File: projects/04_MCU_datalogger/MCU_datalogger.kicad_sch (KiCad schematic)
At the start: 25 parts, among them U1 24LC1025, U2 DS1337S_, U3 24LC1025, U4 ATMEGA328P-AU, Y1 32.768KHz, Y2 16MHz

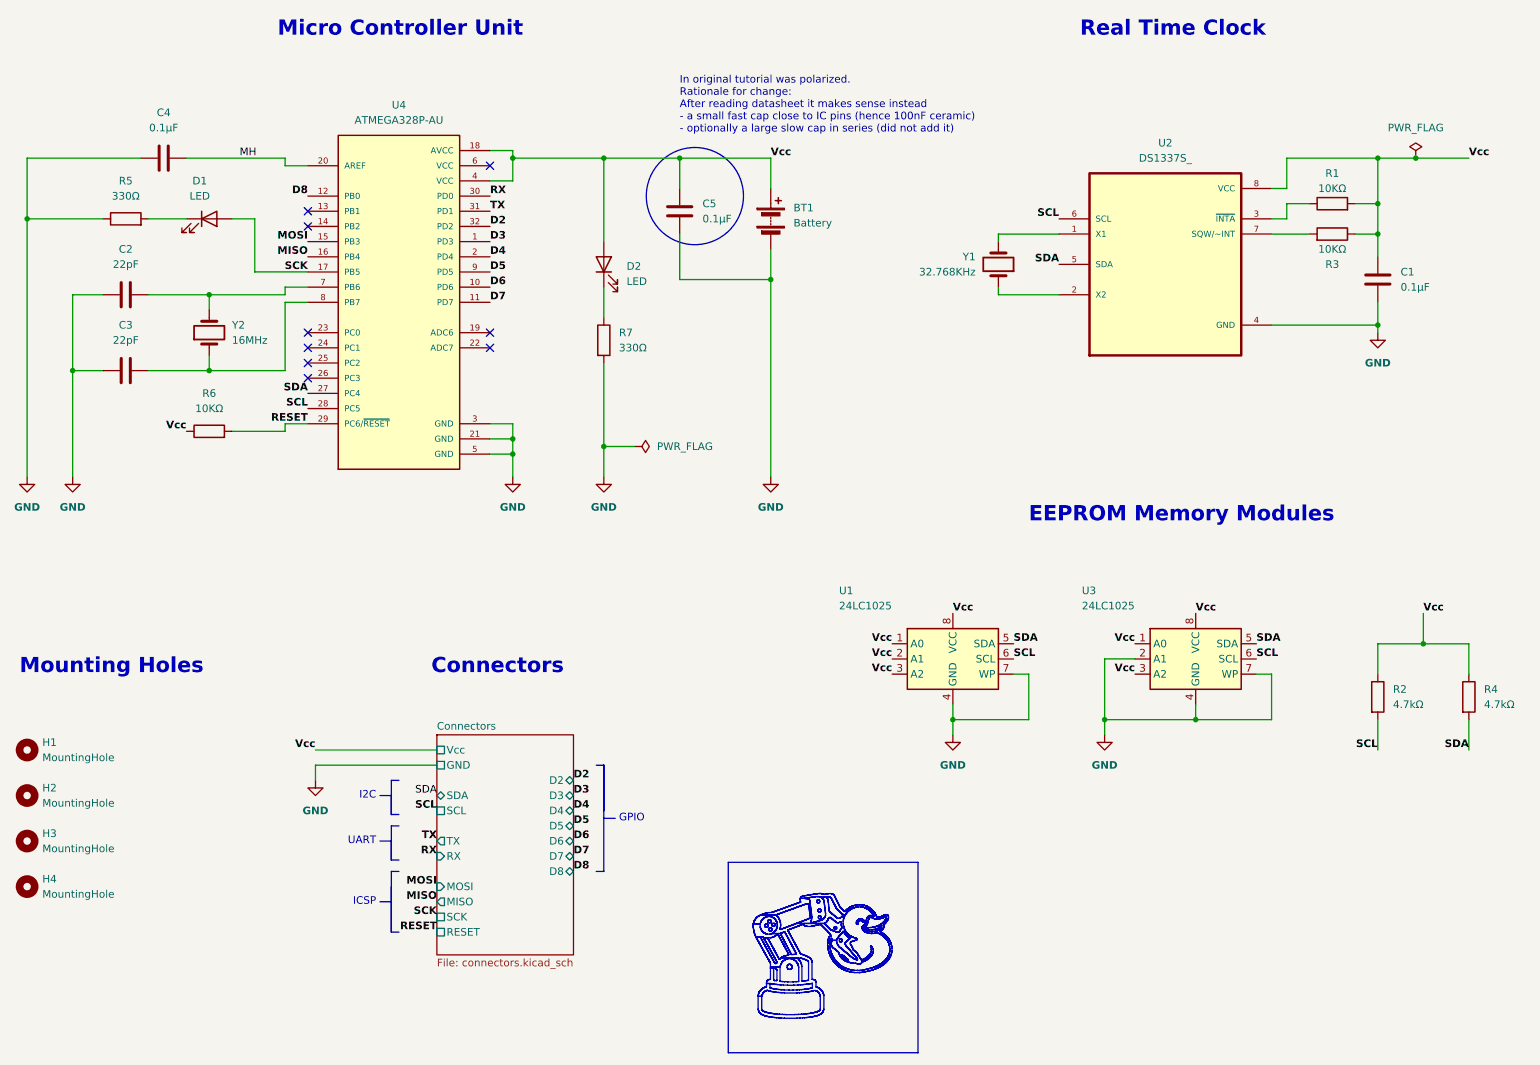
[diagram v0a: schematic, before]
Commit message: MCU datalogger - clean up schematic
In `MCU_datalogger.kicad_sch` and `connectors.kicad_sch`:
- update RTC, EEPROM, Crystal symbols to arrange pins properly
  and align to 100 mil grid
- clean up schematic
- rename nets to start with ICSP_* I2C_* UART_*
- replace Vcc label with VCC power symbol
- add net colors

In `MCU_datalogger.kicad_pcb`:
- replace layout in main branch with empty placeholder referring to 2layer and 4layer branches

Notes:
- ensure modified symbols are saved in custom library (e.g. MH_library)
- before deleting the layout DRC threw hundreds of errors: unconnected pins, solder mask bridges, etc. (WHY?)
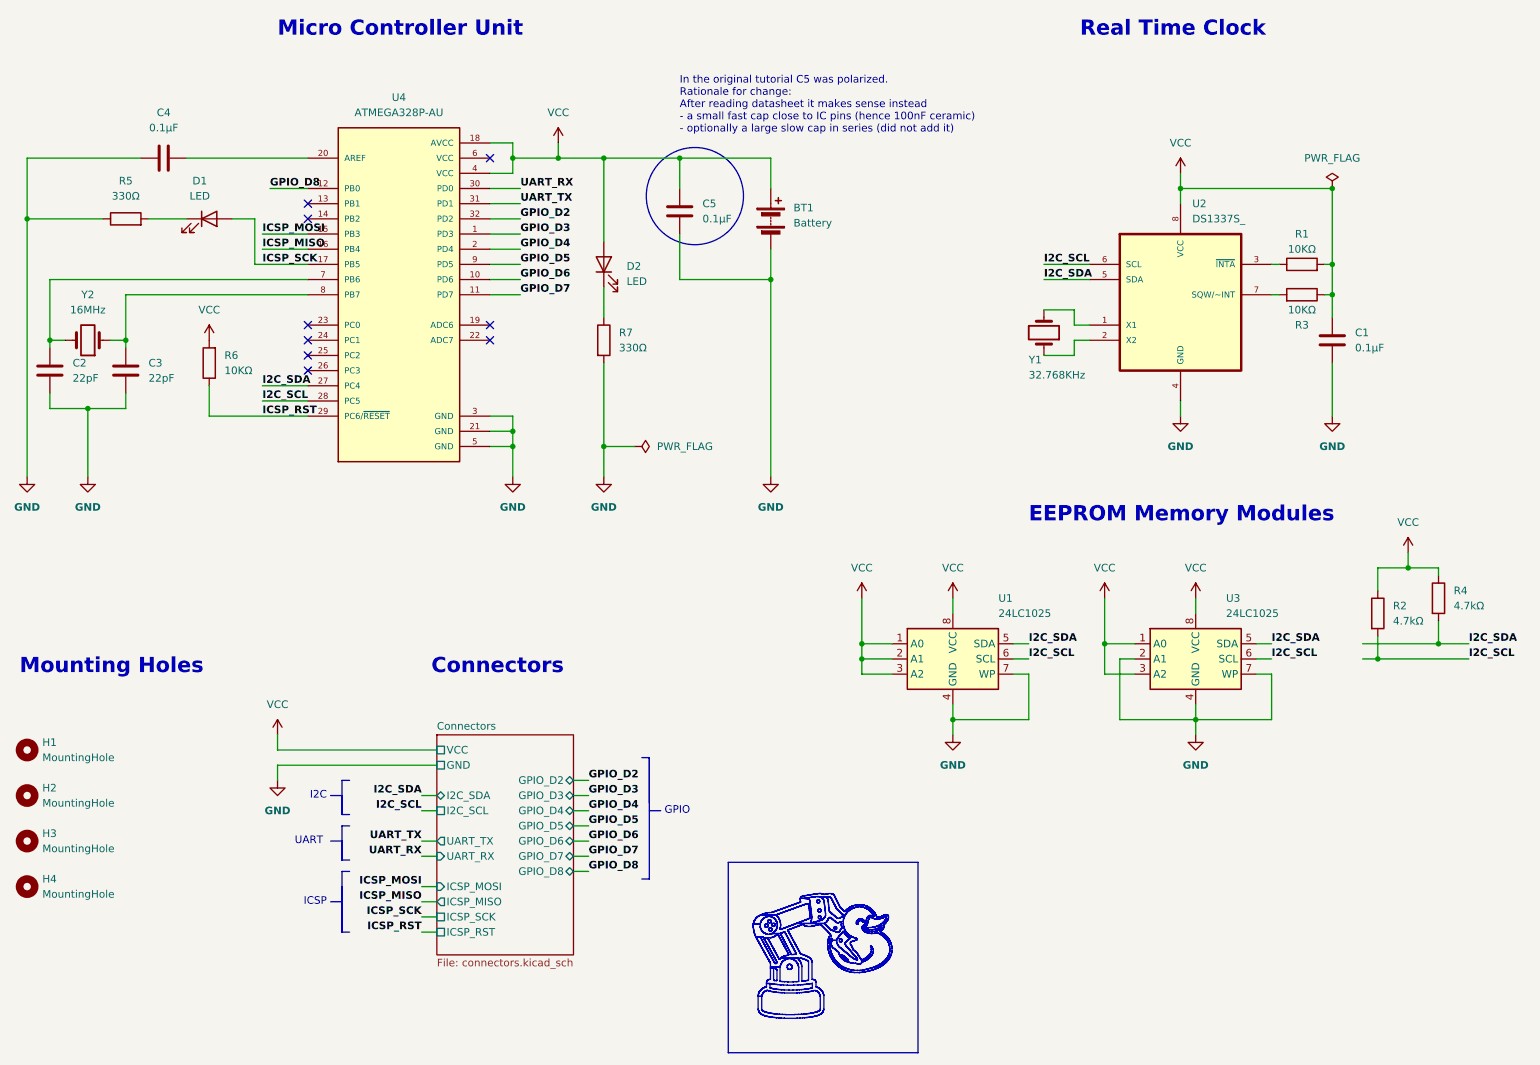
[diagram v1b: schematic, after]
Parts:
- U2: Check_prices https://www.snapeda.com/parts/DS1337S+/Analog+Devices/view-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 -> (none)
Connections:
- net D2 renamed GPIO_D2
- net D3 renamed GPIO_D3
- net D4 renamed GPIO_D4
- net D5 renamed GPIO_D5
- net D6 renamed GPIO_D6
- net D7 renamed GPIO_D7
- net D8 renamed GPIO_D8
- net MH: no longer names the net of C4.2, U4.20 (AREF)
- net MISO renamed ICSP_MISO
- net MOSI renamed ICSP_MOSI
- net RESET renamed ICSP_RST
- net ICSP_RST: now also R6.1; no longer R6.2
- net RX renamed UART_RX
- net SCK renamed ICSP_SCK
- net SCL renamed I2C_SCL
- net SDA renamed I2C_SDA
- net TX renamed UART_TX
- net Vcc renamed VCC
- net VCC: now also R6.2; no longer R6.1
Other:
- sheet Connectors ports: added GPIO_D2, GPIO_D3, GPIO_D4, GPIO_D5, GPIO_D6, GPIO_D7, GPIO_D8, I2C_SCL, I2C_SDA, ICSP_MISO, ICSP_MOSI, ICSP_RST, ICSP_SCK, UART_RX, UART_TX, VCC; removed D2, D3, D4, D5, D6, D7, D8, MISO, MOSI, RESET, RX, SCK, SCL, SDA, TX, Vcc
- note added: "In the original tutorial C5 was polarized. Rationale for change: After reading datasheet it makes sense instead - a small fast cap close to IC pins (hence 100nF ceramic) - optionally a large slow cap in series (did not add it)"
- note removed: "In original tutorial was polarized. Rationale for change: After reading datasheet it makes sense instead - a small fast cap close to IC pins (hence 100nF ceramic) - optionally a large slow cap in series (did not add it)"
- moved on the sheet: C1, C2, C3, R1, R2, R3, R4, R6, U2, U4, Y1, Y2
